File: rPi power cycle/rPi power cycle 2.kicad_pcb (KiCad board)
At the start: 2 copper layers, 53.3 x 25.4 mm, 9 parts, among them J1 RPi GPIO, J2 BATT, J3 RPi PWR, Q1 BC548

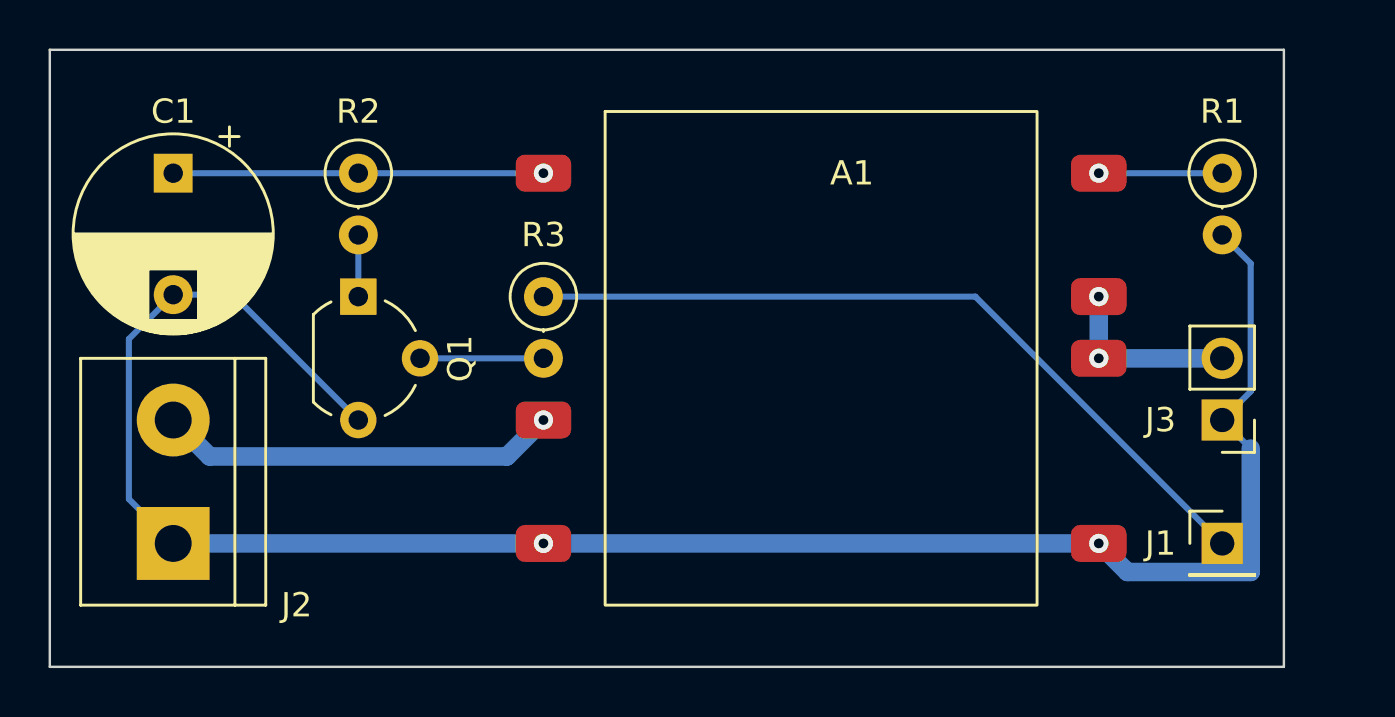
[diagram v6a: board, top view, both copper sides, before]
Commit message: Move GPIO input pin
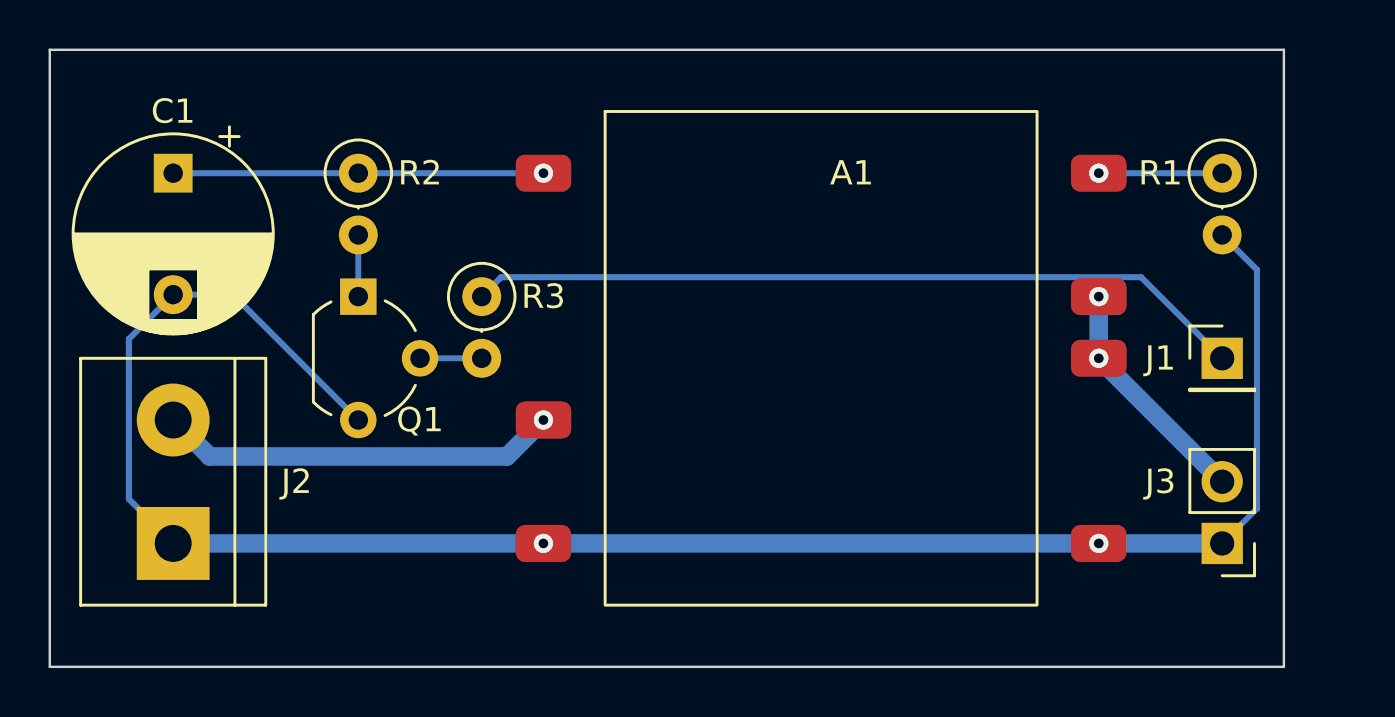
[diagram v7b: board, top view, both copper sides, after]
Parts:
- moved J1 7.62 mm to (132.1, 88.9)
- moved J3 5.08 mm to (132.1, 96.5)
- moved R3 2.54 mm to (101.6, 86.4)
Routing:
- net GND: track 81.7 -> 78.6 mm
- net Net-(Q1-Pad2): track 5.08 -> 2.54 mm
- net +5V: track 7.62 -> 9.72 mm
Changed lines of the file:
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@@
     (property "Sheetname" "")
     (attr through_hole)
-    (fp_text reference "Q1" (at 2.55 -4.19 -90) (layer "F.SilkS")
+    (fp_text reference "Q1" (at 5.08 -2.54 -180) (layer "F.SilkS")
       (effects (font (size 1 1) (thickness 0.15)))
     )
@@
   )
   (footprint "Connector_PinHeader_2.54mm:PinHeader_1x01_P2.54mm_Vertical" (layer "F.Cu")
-    (at 132.08 96.52)
+    (at 132.08 88.9)
     (descr "Through hole straight pin header, 1x01, 2.54mm pitch, single row")
     (tags "Through hole pin header THT 1x01 2.54mm single row")
@@
     (property "Sheetname" "")
     (attr through_hole)
-    (fp_text reference "J2" (at -2.54 5.08) (layer "F.SilkS")
+    (fp_text reference "J2" (at 2.54 5.08) (layer "F.SilkS")
       (effects (font (size 1 1) (thickness 0.15)))
     )
@@
     (property "Sheetname" "")
     (attr through_hole)
-    (fp_text reference "R1" (at -2.54 0) (layer "F.SilkS")
+    (fp_text reference "R1" (at 0 2.54) (layer "F.SilkS")
       (effects (font (size 1 1) (thickness 0.15)))
     )
@@
       (effects (font (size 1 1) (thickness 0.15)))
     )
-    (fp_text user "${REFERENCE}" (at 1.27 -2.37 -270) (layer "F.Fab")
+    (fp_text user "${REFERENCE}" (at 1.27 -2.37 90) (layer "F.Fab")
       (effects (font (size 1 1) (thickness 0.15)))
     )
@@
   )
   (footprint "Connector_PinHeader_2.54mm:PinHeader_1x02_P2.54mm_Vertical" (layer "F.Cu")
-    (at 132.08 91.44 180)
+    (at 132.08 96.52 180)
     (descr "Through hole straight pin header, 1x02, 2.54mm pitch, single row")
     (tags "Through hole pin header THT 1x02 2.54mm single row")
@@
     (property "Sheetname" "")
     (attr through_hole)
-    (fp_text reference "J3" (at 2.54 0 180) (layer "F.SilkS")
+    (fp_text reference "J3" (at 2.54 2.54 180) (layer "F.SilkS")
       (effects (font (size 1 1) (thickness 0.15)))
     )
@@
     (property "Sheetname" "")
     (attr through_hole)
-    (fp_text reference "R2" (at -2.54 0) (layer "F.SilkS")
+    (fp_text reference "R2" (at 0 -2.54) (layer "F.SilkS")
       (effects (font (size 1 1) (thickness 0.15)))
     )
@@
   )
   (footprint "Resistor_THT:R_Axial_DIN0207_L6.3mm_D2.5mm_P2.54mm_Vertical" (layer "F.Cu")
-    (at 104.14 86.36 -90)
+    (at 101.6 86.36 -90)
     (descr "Resistor, Axial_DIN0207 series, Axial, Vertical, pin pitch=2.54mm, 0.25W = 1/4W, length*diameter=6.3*2.5mm^2, http://cdn-reichelt.de/documents/datenblatt/B400/1_4W%23YAG.pdf")
     (tags "Resistor Axial_DIN0207 series Axial Vertical pin pitch 2.54mm 0.25W = 1/4W length 6.3mm diameter 2.5mm")
@@
     (property "Sheetname" "")
     (attr through_hole)
-    (fp_text reference "R3" (at -2.54 0) (layer "F.SilkS")
+    (fp_text reference "R3" (at 0 -2.54) (layer "F.SilkS")
       (effects (font (size 1 1) (thickness 0.15)))
     )
@@
   (via (at 104.14 96.52) (size 0.8) (drill 0.4) (layers "F.Cu" "B.Cu") (net 3))
   (via (at 127 96.52) (size 0.8) (drill 0.4) (layers "F.Cu" "B.Cu") (net 3))
-  (segment (start 127 96.52) (end 128.174511 97.694511) (width 0.762) (layer "B.Cu") (net 3))
   (segment (start 88.9 86.28) (end 91.36 86.28) (width 0.25) (layer "B.Cu") (net 3))
-  (segment (start 133.254511 97.694511) (end 133.254511 92.614511) (width 0.762) (layer "B.Cu") (net 3))
-  (segment (start 133.254511 90.265489) (end 133.254511 84.994511) (width 0.25) (layer "B.Cu") (net 3))
+  (segment (start 132.08 83.82) (end 133.510511 85.250511) (width 0.249987) (layer "B.Cu") (net 3))
+  (segment (start 133.510511 95.089489) (end 132.08 96.52) (width 0.249987) (layer "B.Cu") (net 3))
   (segment (start 88.9 96.52) (end 104.14 96.52) (width 0.762) (layer "B.Cu") (net 3))
   (segment (start 104.14 96.52) (end 127 96.52) (width 0.762) (layer "B.Cu") (net 3))
   (segment (start 87.075489 88.104511) (end 88.9 86.28) (width 0.25) (layer "B.Cu") (net 3))
+  (segment (start 127 96.52) (end 132.08 96.52) (width 0.762) (layer "B.Cu") (net 3))
   (segment (start 87.075489 94.695489) (end 87.075489 88.104511) (width 0.25) (layer "B.Cu") (net 3))
-  (segment (start 128.174511 97.694511) (end 133.254511 97.694511) (width 0.762) (layer "B.Cu") (net 3))
   (segment (start 88.9 96.52) (end 87.075489 94.695489) (width 0.25) (layer "B.Cu") (net 3))
-  (segment (start 133.254511 84.994511) (end 132.08 83.82) (width 0.25) (layer "B.Cu") (net 3))
+  (segment (start 133.510511 85.250511) (end 133.510511 95.089489) (width 0.249987) (layer "B.Cu") (net 3))
   (segment (start 91.36 86.28) (end 96.52 91.44) (width 0.25) (layer "B.Cu") (net 3))
-  (segment (start 132.08 91.44) (end 133.254511 90.265489) (width 0.25) (layer "B.Cu") (net 3))
-  (segment (start 133.254511 92.614511) (end 132.08 91.44) (width 0.25) (layer "B.Cu") (net 3))
   (via (at 127 81.28) (size 0.8) (drill 0.4) (layers "F.Cu" "B.Cu") (net 4))
   (segment (start 127 81.28) (end 132.08 81.28) (width 0.25) (layer "B.Cu") (net 4))
   (via (at 127 88.9) (size 0.8) (drill 0.4) (layers "F.Cu" "B.Cu") (net 5))
   (via (at 127 86.36) (size 0.8) (drill 0.4) (layers "F.Cu" "B.Cu") (net 5))
-  (segment (start 127 88.9) (end 132.08 88.9) (width 0.762) (layer "B.Cu") (net 5))
   (segment (start 127 86.36) (end 127 88.9) (width 0.762) (layer "B.Cu") (net 5))
-  (segment (start 132.08 96.52) (end 121.92 86.36) (width 0.25) (layer "B.Cu") (net 6))
-  (segment (start 121.92 86.36) (end 104.14 86.36) (width 0.25) (layer "B.Cu") (net 6))
+  (segment (start 127 88.9) (end 132.08 93.98) (width 0.762) (layer "B.Cu") (net 5))
+  (segment (start 128.740001 85.560001) (end 132.08 88.9) (width 0.25) (layer "B.Cu") (net 6))
+  (segment (start 101.6 86.36) (end 102.399999 85.560001) (width 0.25) (layer "B.Cu") (net 6))
+  (segment (start 102.399999 85.560001) (end 128.740001 85.560001) (width 0.25) (layer "B.Cu") (net 6))
   (segment (start 96.52 86.36) (end 96.52 83.82) (width 0.25) (layer "B.Cu") (net 7))
-  (segment (start 104.14 88.9) (end 99.06 88.9) (width 0.25) (layer "B.Cu") (net 8))
+  (segment (start 99.06 88.9) (end 101.6 88.9) (width 0.25) (layer "B.Cu") (net 8))
 )
